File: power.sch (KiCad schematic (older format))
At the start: 17 parts, among them J6 Barrel_Jack_MountingPin, Q3 AO3401A, SW3 SW_SPST, U1 AMS1117-3.3, U4 MC33269DT−5.0, U5 LM358

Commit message: Reorganize symbols & update vendors
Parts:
- C5: renamed from C1; value C -> 22uF; Vendor (none) -> tme.eu; VendorLink (none) -> https://www.tme.eu/pl/details/cl21a226mqqnnng/kondensatory-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
- C6: renamed from C2; value C -> 22uF; Vendor (none) -> tme.eu; VendorLink (none) -> https://www.tme.eu/pl/details/cl21a226mqqnnng/kondensatory-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
- C7, C8: value CP -> 47uF; Vendor (none) -> tme.eu; VendorLink (none) -> https://www.tme.eu/pl/details/ck1c476m05005vr/kondensatory-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
- C9: value C -> 100nF; Vendor (none) -> avt.pl; VendorLink (none) -> https://sklep.avt.pl/zestaw-kondensatorow-smd-0805-720-sztu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
- D1: value D -> M7; footprint Diode_SMD:D_0805_2012Metric_Pad1.15x1.40mm_HandSolder -> Diode_SMD:D_SMA_Handsoldering; Vendor (none) -> tme.eu; VendorLink (none) -> https://www.tme.eu/pl/details/m7-dio/diody-uniwersalne-smd/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
- D2: renamed from D3; value LED -> RF-GSS150TS-BC; Vendor (none) -> tme.eu; VendorLink (none) -> https://www.tme.eu/pl/details/rf-gss150ts-bc/diody-led-smd-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
- D3: renamed from D2; value D_Schottky -> STPS0520Z; Vendor (none) -> tme.eu; VendorLink (none) -> https://www.tme.eu/pl/details/stps0520z/diody-schottky-smd/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
- Q1: renamed from Q3; value AO3401A -> ?
- R1: renamed from R5; Vendor (none) -> avt.pl; VendorLink (none) -> https://sklep.avt.pl/avt701-805.html
- R2: renamed from R8; Vendor (none) -> avt.pl; VendorLink (none) -> https://sklep.avt.pl/avt701-805.html
- R3: value ? Ohm -> 220 Ohm; Vendor (none) -> avt.pl; VendorLink (none) -> https://sklep.avt.pl/avt701-805.html
- renumbered J6 to J5, U5 to U2, U1 to U3

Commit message: Remove Op-Amp circuit for USB power
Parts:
- removed D3: STPS0520Z, Diode_SMD:D_0805_2012Metric_Pad1.15x1.40mm_HandSolder, symbol Device:D_Schottky
- removed Q1: ?, Package_TO_SOT_SMD:SOT-23, symbol Transistor_FET:AO3401A
- removed R1, R2: 10k Ohm, Resistor_SMD:R_0805_2012Metric_Pad1.20x1.40mm_HandSolder, symbol Device:R
- removed U2: LM358, Package_SO:SOP-8_3.76x4.96mm_P1.27mm, symbol Amplifier_Operational:LM358
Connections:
- net labels removed: VBUS
- wire segments 56 -> 39
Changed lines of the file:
@@
 Text HLabel 2850 1300 2    50   UnSpc ~ 0
 VIN
-$Comp
-L Device:D_Schottky D?
-U 1 1 5FBD81C3
-P 2900 3700
-AR Path="/5FBD81C3" Ref="D?"  Part="1"
-AR Path="/5FF6344B/5FBD81C3" Ref="D3"  Part="1"
-F 0 "D3" H 2900 3450 50  0000 C CNN
-F 1 "STPS0520Z" H 2900 3550 50  0000 C CNN
-F 2 "Diode_SMD:D_0805_2012Metric_Pad1.15x1.40mm_HandSolder" H 2900 3700 50  0001 C CNN
-F 3 "https://www.st.com/resource/en/datasheet/stps0520z.pdf" H 2900 3700 50  0001 C CNN
-F 4 "tme.eu" H 2900 3700 50  0001 C CNN "Vendor"
-F 5 "https://www.tme.eu/pl/details/stps0520z/diody-schottky-smd/stmicroelectronics/" H 2900 3700 50  0001 C CNN "VendorLink"
-	1    2900 3700
-	-1   0    0    1
-$EndComp
-$Comp
-L Transistor_FET:AO3401A Q?
-U 1 1 5FBD81D8
-P 3350 3600
-AR Path="/5FBD81D8" Ref="Q?"  Part="1"
-AR Path="/5FF6344B/5FBD81D8" Ref="Q1"  Part="1"
-F 0 "Q1" V 3650 3600 50  0000 C CNN
-F 1 "?" V 3750 3600 50  0000 C CNN
-F 2 "Package_TO_SOT_SMD:SOT-23" H 3550 3525 50  0001 L CIN
-F 3 "http://www.aosmd.com/pdfs/datasheet/AO3401A.pdf" H 3350 3600 50  0001 L CNN
-	1    3350 3600
-	0    -1   1    0
-$EndComp
-Wire Wire Line
-	3050 3700 3150 3700
-Wire Wire Line
-	3550 3700 3850 3700
-Wire Wire Line
-	3350 3400 3350 3050
-Wire Wire Line
-	3350 3050 3200 3050
-$Comp
-L Amplifier_Operational:LM358 U?
-U 1 1 5FBD81E2
-P 2900 3050
-AR Path="/5FBD81E2" Ref="U?"  Part="1"
-AR Path="/5FF6344B/5FBD81E2" Ref="U2"  Part="1"
-F 0 "U2" H 2900 3450 50  0000 C CNN
-F 1 "LM358" H 2900 3350 50  0000 C CNN
-F 2 "Package_SO:SOP-8_3.76x4.96mm_P1.27mm" H 2900 3050 50  0001 C CNN
-F 3 "http://www.ti.com/lit/ds/symlink/lm2904-n.pdf" H 2900 3050 50  0001 C CNN
-	1    2900 3050
-	1    0    0    -1
-$EndComp
-Wire Wire Line
-	2500 2350 2500 3150
-Wire Wire Line
-	2500 3150 2600 3150
-Wire Wire Line
-	2600 2950 2250 2950
-$Comp
-L Device:R R?
-U 1 1 5FBD81F1
-P 2250 2750
-AR Path="/5FBD81F1" Ref="R?"  Part="1"
-AR Path="/5FF6344B/5FBD81F1" Ref="R1"  Part="1"
-F 0 "R1" H 2050 2850 50  0000 L CNN
-F 1 "10k Ohm" H 1850 2750 50  0000 L CNN
-F 2 "Resistor_SMD:R_0805_2012Metric_Pad1.20x1.40mm_HandSolder" V 2180 2750 50  0001 C CNN
-F 3 "~" H 2250 2750 50  0001 C CNN
-F 4 "avt.pl" H 2250 2750 50  0001 C CNN "Vendor"
-F 5 "https://sklep.avt.pl/avt701-805.html" H 2250 2750 50  0001 C CNN "VendorLink"
-	1    2250 2750
-	1    0    0    -1
-$EndComp
-$Comp
-L Device:R R?
-U 1 1 5FBD81F7
-P 2250 3150
-AR Path="/5FBD81F7" Ref="R?"  Part="1"
-AR Path="/5FF6344B/5FBD81F7" Ref="R2"  Part="1"
-F 0 "R2" H 2050 3200 50  0000 L CNN
-F 1 "10k Ohm" H 1850 3100 50  0000 L CNN
-F 2 "Resistor_SMD:R_0805_2012Metric_Pad1.20x1.40mm_HandSolder" V 2180 3150 50  0001 C CNN
-F 3 "~" H 2250 3150 50  0001 C CNN
-F 4 "avt.pl" H 2250 3150 50  0001 C CNN "Vendor"
-F 5 "https://sklep.avt.pl/avt701-805.html" H 2250 3150 50  0001 C CNN "VendorLink"
-	1    2250 3150
-	1    0    0    -1
-$EndComp
-Wire Wire Line
-	2250 2900 2250 2950
-Wire Wire Line
-	2250 2950 2250 3000
-Connection ~ 2250 2950
-Wire Wire Line
-	1350 2550 2250 2550
-Wire Wire Line
-	2250 2550 2250 2600
-$Comp
-L power:GND #PWR?
-U 1 1 5FBD8203
-P 2250 3950
-AR Path="/5FBD8203" Ref="#PWR?"  Part="1"
-AR Path="/5FF6344B/5FBD8203" Ref="#PWR021"  Part="1"
-F 0 "#PWR021" H 2250 3700 50  0001 C CNN
-F 1 "GND" H 2300 3750 50  0000 C CNN
-F 2 "" H 2250 3950 50  0001 C CNN
-F 3 "" H 2250 3950 50  0001 C CNN
-	1    2250 3950
-	1    0    0    -1
-$EndComp
-Wire Wire Line
-	2250 3300 2250 3950
-$Comp
-L Amplifier_Operational:LM358 U?
-U 3 1 5FBD820A
-P 5050 3250
-AR Path="/5FBD820A" Ref="U?"  Part="3"
-AR Path="/5FF6344B/5FBD820A" Ref="U2"  Part="3"
-F 0 "U2" H 5050 3300 50  0000 L CNN
-F 1 "LM358" H 5050 3250 50  0000 L CNN
-F 2 "Package_SO:SOP-8_3.76x4.96mm_P1.27mm" H 5050 3250 50  0001 C CNN
-F 3 "http://www.ti.com/lit/ds/symlink/lm2904-n.pdf" H 5050 3250 50  0001 C CNN
-	3    5050 3250
-	1    0    0    -1
-$EndComp
-$Comp
-L power:GND #PWR?
-U 1 1 5FBD8216
-P 4950 3950
-AR Path="/5FBD8216" Ref="#PWR?"  Part="1"
-AR Path="/5FF6344B/5FBD8216" Ref="#PWR023"  Part="1"
-F 0 "#PWR023" H 4950 3700 50  0001 C CNN
-F 1 "GND" H 5000 3750 50  0000 C CNN
-F 2 "" H 4950 3950 50  0001 C CNN
-F 3 "" H 4950 3950 50  0001 C CNN
-	1    4950 3950
-	1    0    0    -1
-$EndComp
-Wire Wire Line
-	4950 2550 4950 2950
-Wire Wire Line
-	4950 3550 4950 3950
 Text HLabel 7650 1400 2    50   UnSpc ~ 0
 +5V
@@
 Text HLabel 5350 1400 0    50   UnSpc ~ 0
 VIN
-Text HLabel 1350 2550 0    50   UnSpc ~ 0
-VIN
-Text HLabel 1350 3700 0    50   UnSpc ~ 0
-VBUS
-Wire Wire Line
-	1350 3700 2750 3700
-Text HLabel 3850 3700 2    50   UnSpc ~ 0
-+5V
-Text HLabel 4850 2550 0    50   UnSpc ~ 0
-+5V
-Wire Wire Line
-	4850 2550 4950 2550
 $Comp
 L Regulator_Linear:AMS1117-3.3 U?
@@
 Wire Wire Line
 	7800 5600 7900 5600
-Wire Wire Line
-	1350 2350 2500 2350
-Text HLabel 1350 2350 0    50   UnSpc ~ 0
-Internal_3V3
 $EndSCHEMATC

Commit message: Change regulators to NCP1117ST50T3G/NCP1117-3.3
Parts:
- U3: value AMS1117-3.3 -> NCP1117-3.3; symbol Regulator_Linear:AMS1117-3.3 -> Regulator_Linear:NCP1117-3.3_SOT223; Vendor (none) -> tme.eu; VendorLink (none) -> https://www.tme.eu/pl/details/ncp1117st33t3g/stabilizatory-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
- U4: value MC33269DT−5.0 -> NCP1117ST50T3G; footprint Package_TO_SOT_SMD:TO-252-2 -> Package_TO_SOT_SMD:SOT-223-3_TabPin2; symbol Regulator_Linear:MC33269DT−5.0 -> Regulator_Linear:NCP1117-5.0_SOT223; Vendor (none) -> tme.eu; VendorLink (none) -> https://www.tme.eu/pl/details/ncp1117st50t3g/stabilizatory-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
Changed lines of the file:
@@
 $EndComp
 $Comp
-L Regulator_Linear:MC33269DT−5.0 U?
+L Regulator_Linear:NCP1117-5.0_SOT223 U?
 U 1 1 5FB78036
 P 6250 1400
@@
 AR Path="/5FF6344B/5FB78036" Ref="U4"  Part="1"
 F 0 "U4" H 6250 1700 50  0000 C CNN
-F 1 "MC33269DT−5.0" H 6250 1600 50  0000 C CNN
-F 2 "Package_TO_SOT_SMD:TO-252-2" H 6250 1625 50  0001 C CIN
-F 3 "https://www.onsemi.com/pub/Collateral/MC33269-D.PDF" H 6250 1350 50  0001 C CNN
+F 1 "NCP1117ST50T3G" H 6250 1600 50  0000 C CNN
+F 2 "Package_TO_SOT_SMD:SOT-223-3_TabPin2" H 6250 1625 50  0001 C CIN
+F 3 "http://www.onsemi.com/pub_link/Collateral/NCP1117-D.PDF" H 6250 1350 50  0001 C CNN
+F 4 "tme.eu" H 6250 1400 50  0001 C CNN "Vendor"
+F 5 "https://www.tme.eu/pl/details/ncp1117st50t3g/stabilizatory-napiecia-nieregulowane-ldo/on-semiconductor/" H 6250 1400 50  0001 C CNN "VendorLink"
 	1    6250 1400
 	1    0    0    -1
@@
 $EndComp
 $Comp
-L Regulator_Linear:AMS1117-3.3 U?
+L Regulator_Linear:NCP1117-3.3_SOT223 U?
 U 1 1 5FD3645F
 P 3550 5550
@@
 AR Path="/5FF6344B/5FD3645F" Ref="U3"  Part="1"
 F 0 "U3" H 3550 5850 50  0000 C CNN
-F 1 "AMS1117-3.3" H 3550 5750 50  0000 C CNN
+F 1 "NCP1117-3.3" H 3550 5750 50  0000 C CNN
 F 2 "Package_TO_SOT_SMD:SOT-223-3_TabPin2" H 3550 5750 50  0001 C CNN
 F 3 "http://www.advanced-monolithic.com/pdf/ds1117.pdf" H 3650 5300 50  0001 C CNN
+F 4 "tme.eu" H 3550 5550 50  0001 C CNN "Vendor"
+F 5 "https://www.tme.eu/pl/details/ncp1117st33t3g/stabilizatory-napiecia-nieregulowane-ldo/on-semiconductor/" H 3550 5550 50  0001 C CNN "VendorLink"
 	1    3550 5550
 	1    0    0    -1

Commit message: Update DC connector
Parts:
- J5: footprint Connector_BarrelJack:BarrelJack_CLIFF_FC681465S_SMT_Horizontal -> Connector_BarrelJack:BarrelJack_Lumberg_1613-21_Horizontal; symbol Connector:Barrel_Jack -> Connector:Barrel_Jack_Switch; Vendor (none) -> tme.eu; VendorLink (none) -> https://www.tme.eu/pl/details/1613-21/zlacza-dc/lumberg/161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
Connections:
- net GND: now also J5.2, J5.3; no longer J5.1
- net at D1.2 (A): now also J5.1; no longer J5.2
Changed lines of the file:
@@
 $EndDescr
 $Comp
-L Connector:Barrel_Jack J?
+L Connector:Barrel_Jack_Switch J?
 U 1 1 5FB78030
 P 1600 1400
@@
 F 0 "J5" H 1350 1150 50  0000 C CNN
 F 1 "Barrel_Jack_MountingPin" H 1550 1650 50  0000 C CNN
-F 2 "Connector_BarrelJack:BarrelJack_CLIFF_FC681465S_SMT_Horizontal" H 1650 1360 50  0001 C CNN
-F 3 "~" H 1650 1360 50  0001 C CNN
+F 2 "Connector_BarrelJack:BarrelJack_Lumberg_1613-21_Horizontal" H 1650 1360 50  0001 C CNN
+F 3 "https://www.tme.eu/Document/3d585bc2823a1d150d9d924b483e2fef/1613-21.pdf" H 1650 1360 50  0001 C CNN
+F 4 "tme.eu" H 1600 1400 50  0001 C CNN "Vendor"
+F 5 "https://www.tme.eu/pl/details/1613-21/zlacza-dc/lumberg/1613-21/" H 1600 1400 50  0001 C CNN "VendorLink"
 	1    1600 1400
-	1    0    0    1
+	1    0    0    -1
 $EndComp
 $Comp
@@
 L power:GND #PWR?
 U 1 1 5FB78076
-P 2100 1850
+P 2100 1750
 AR Path="/5FB78076" Ref="#PWR?"  Part="1"
 AR Path="/5FF6344B/5FB78076" Ref="#PWR020"  Part="1"
-F 0 "#PWR020" H 2100 1600 50  0001 C CNN
-F 1 "GND" H 2150 1650 50  0000 C CNN
-F 2 "" H 2100 1850 50  0001 C CNN
-F 3 "" H 2100 1850 50  0001 C CNN
-	1    2100 1850
+F 0 "#PWR020" H 2100 1500 50  0001 C CNN
+F 1 "GND" H 2150 1550 50  0000 C CNN
+F 2 "" H 2100 1750 50  0001 C CNN
+F 3 "" H 2100 1750 50  0001 C CNN
+	1    2100 1750
 	1    0    0    -1
 $EndComp
@@
 	2450 1300 2850 1300
 Wire Wire Line
-	1900 1500 2100 1500
-Wire Wire Line
-	2100 1500 2100 1850
+	1900 1400 2100 1400
+Wire Wire Line
+	2100 1400 2100 1500
 Text HLabel 5350 1400 0    50   UnSpc ~ 0
 VIN
@@
 	1    0    0    -1
 $EndComp
+Wire Wire Line
+	1900 1500 2100 1500
+Connection ~ 2100 1500
+Wire Wire Line
+	2100 1500 2100 1750
 $EndSCHEMATC

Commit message: Update power switch
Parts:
- SW3: value SW_SPST -> SW_DPDT_x2; footprint Button_Switch_SMD:SW_DIP_SPSTx01_Slide_6.7x4.1mm_W6.73mm_P2.54mm_LowProfile_JPin -> Button_Switch_SMD:Nidec_CL-SB-22B-0X; symbol Switch:SW_SPST -> Switch:SW_DPDT_x2; Vendor (none) -> tme.eu; VendorLink (none) -> https://www.tme.eu/pl/details/cl-sb-22b-01/przelaczniki-suw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
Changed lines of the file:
@@
 VIN
 Wire Wire Line
-	7800 5600 7900 5600
+	7800 5500 7900 5500
 Wire Wire Line
-	7300 5600 7400 5600
-Text HLabel 7300 5600 0    50   UnSpc ~ 0
+	7300 5400 7400 5400
+Text HLabel 7300 5400 0    50   UnSpc ~ 0
 Internal_3V3
-Text HLabel 7900 5600 2    50   UnSpc ~ 0
+Text HLabel 7900 5500 2    50   UnSpc ~ 0
 +3.3V
 $Comp
-L Switch:SW_SPST SW3
+L Switch:SW_DPDT_x2 SW3
 U 1 1 5FE84590
-P 7600 5600
-F 0 "SW3" H 7600 5850 50  0000 C CNN
-F 1 "SW_SPST" H 7600 5750 50  0000 C CNN
-F 2 "Button_Switch_SMD:SW_DIP_SPSTx01_Slide_6.7x4.1mm_W6.73mm_P2.54mm_LowProfile_JPin" H 7600 5600 50  0001 C CNN
-F 3 "~" H 7600 5600 50  0001 C CNN
-	1    7600 5600
-	1    0    0    -1
+P 7600 5500
+F 0 "SW3" H 7600 5750 50  0000 C CNN
+F 1 "SW_DPDT_x2" H 7600 5650 50  0000 C CNN
+F 2 "Button_Switch_SMD:Nidec_CL-SB-22B-0X" H 7600 5250 50  0000 C CNN
+F 3 "https://www.tme.eu/Document/3439bdb81b005bcee4b59ba949df073a/seriaCL-SB.pdf" H 7600 5500 50  0001 C CNN
+F 4 "tme.eu" H 7600 5500 50  0001 C CNN "Vendor"
+F 5 "https://www.tme.eu/pl/details/cl-sb-22b-01/przelaczniki-suwakowe/nidec-copal-electronics/" H 7600 5500 50  0001 C CNN "VendorLink"
+	1    7600 5500
+	-1   0    0    -1
 $EndComp
 Connection ~ 4250 5550

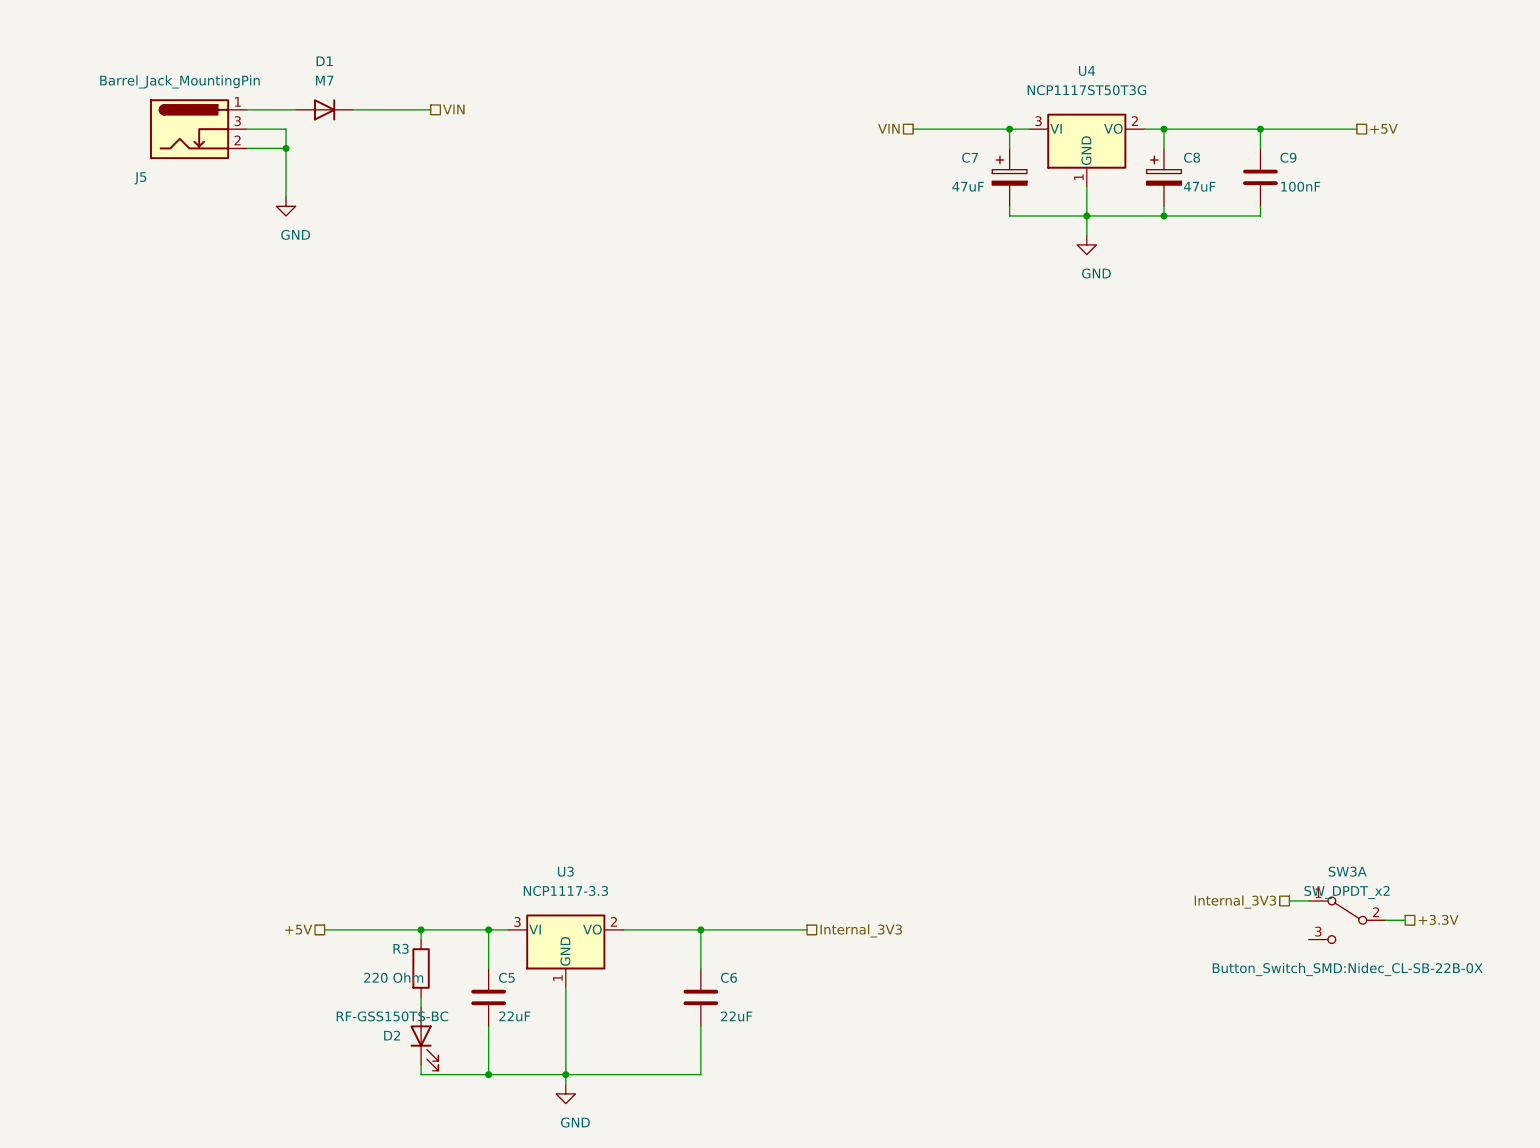
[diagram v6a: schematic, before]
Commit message: Schematic reorganization & reannotate
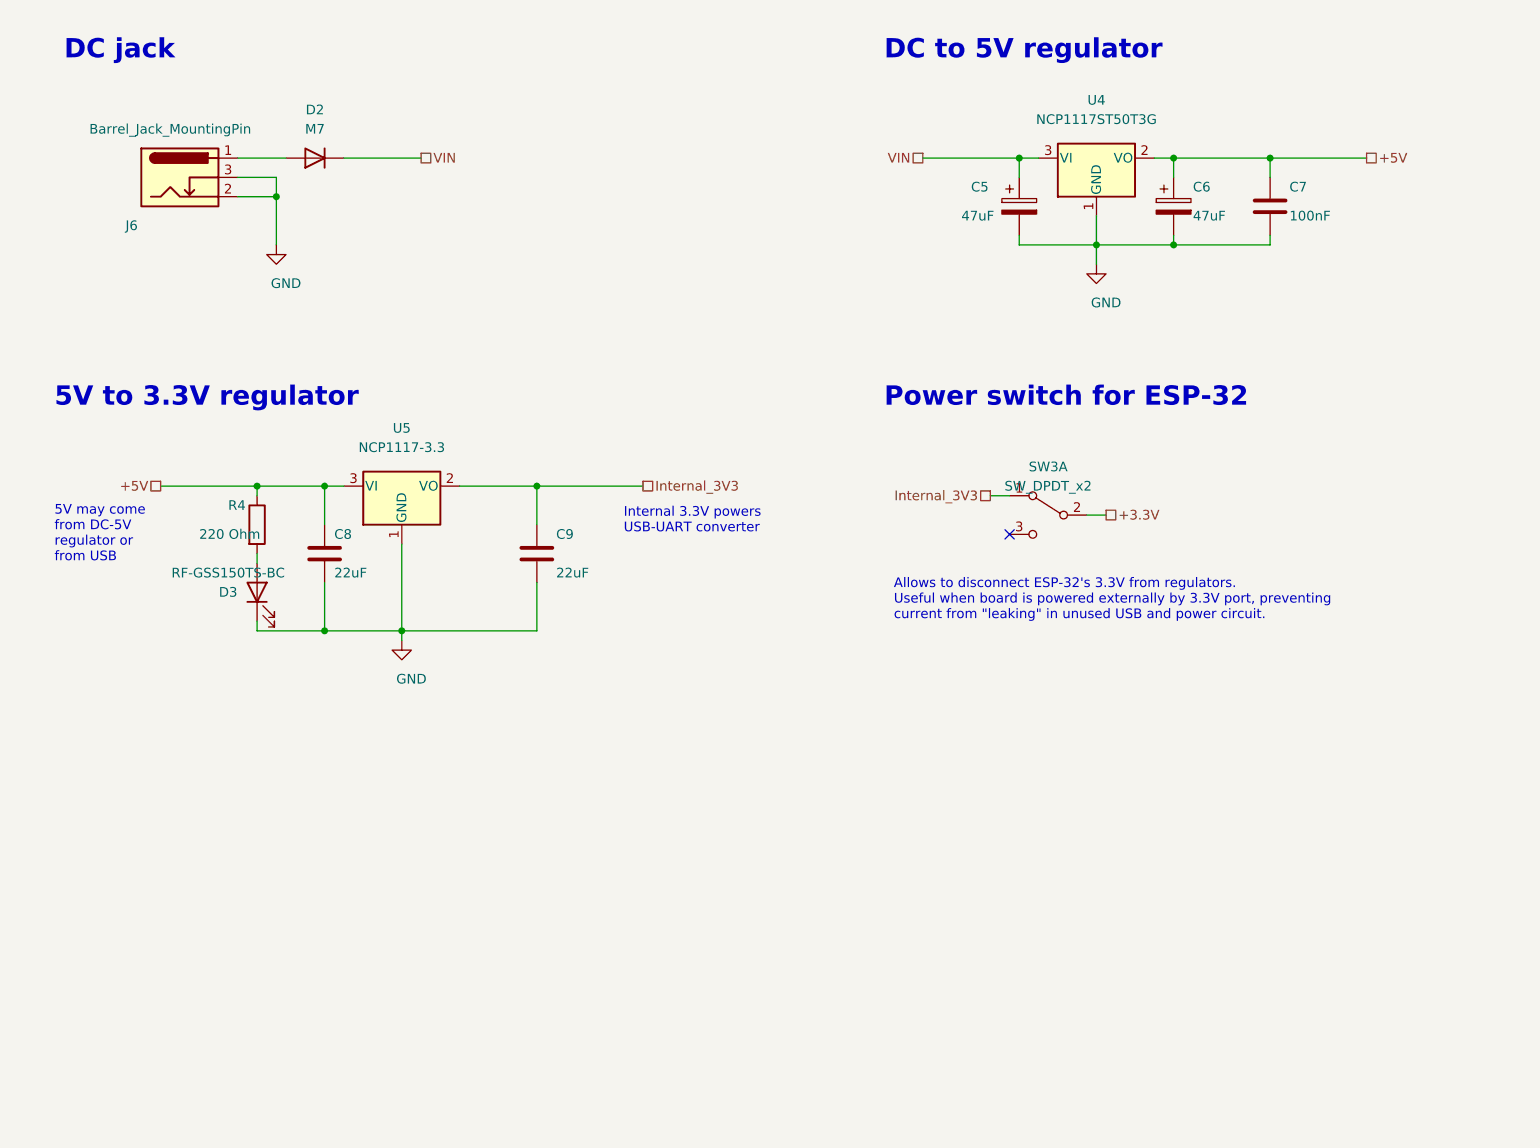
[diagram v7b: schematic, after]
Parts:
- renumbered C7 to C5, C8 to C6, C9 to C7, C5 to C8, C6 to C9, D1 to D2, D2 to D3, J5 to J6, R3 to R4, U3 to U5
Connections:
- no-connect marks 0 -> 1
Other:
- note added: "5V may come\nfrom DC-5V\nregulator or\nfrom USB"
- note added: "5V to 3.3V regulator"
- note added: "Allows to disconnect ESP-32's 3.3V from regulators.\nUseful when board is powered externally by 3.3V port, preventing\ncurrent from "leaking" in unused USB and power circuit."
- note added: "DC jack"
- note added: "DC to 5V regulator"
- note added: "Internal 3.3V powers\nUSB-UART converter"
- note added: "Power switch for ESP-32"
- moved on the sheet: C5, C6, C7, C8, C9, D2, D3, J6, R4, SW3A, U4, U5
